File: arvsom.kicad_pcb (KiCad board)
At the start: 12 copper layers, 55 x 40 mm, 414 parts, among them J3 DF40C-100DP-0.4V(51), J4 DF40C-100DP-0.4V(51), Q5 BSS138AKA, U1 MT53D1024M32D4DT-053, U10 TDA19988BHN_C1,557, U11 KSZ9031RNXCA, U13 VIC7100, U2 GD25LQ256DWIGR, U3 MT53D1024M32D4DT-053, U4 CSD86330Q3D, U5 LMR62014XMF_NOPB, U6 CSD86330Q3D, U8 TPS65086100, Y1 ABM8G-25.000MHZ-18-D2Y-T

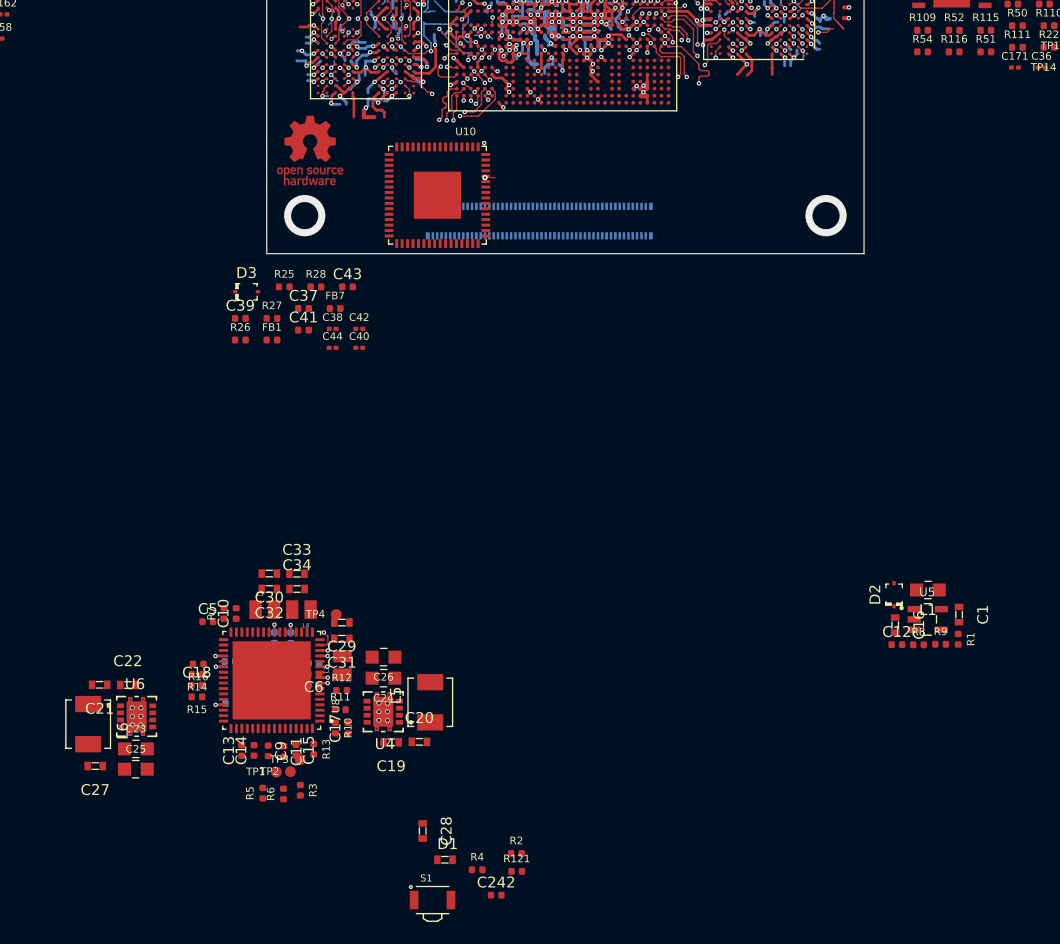
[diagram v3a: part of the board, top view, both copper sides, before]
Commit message: PMIC initial placement
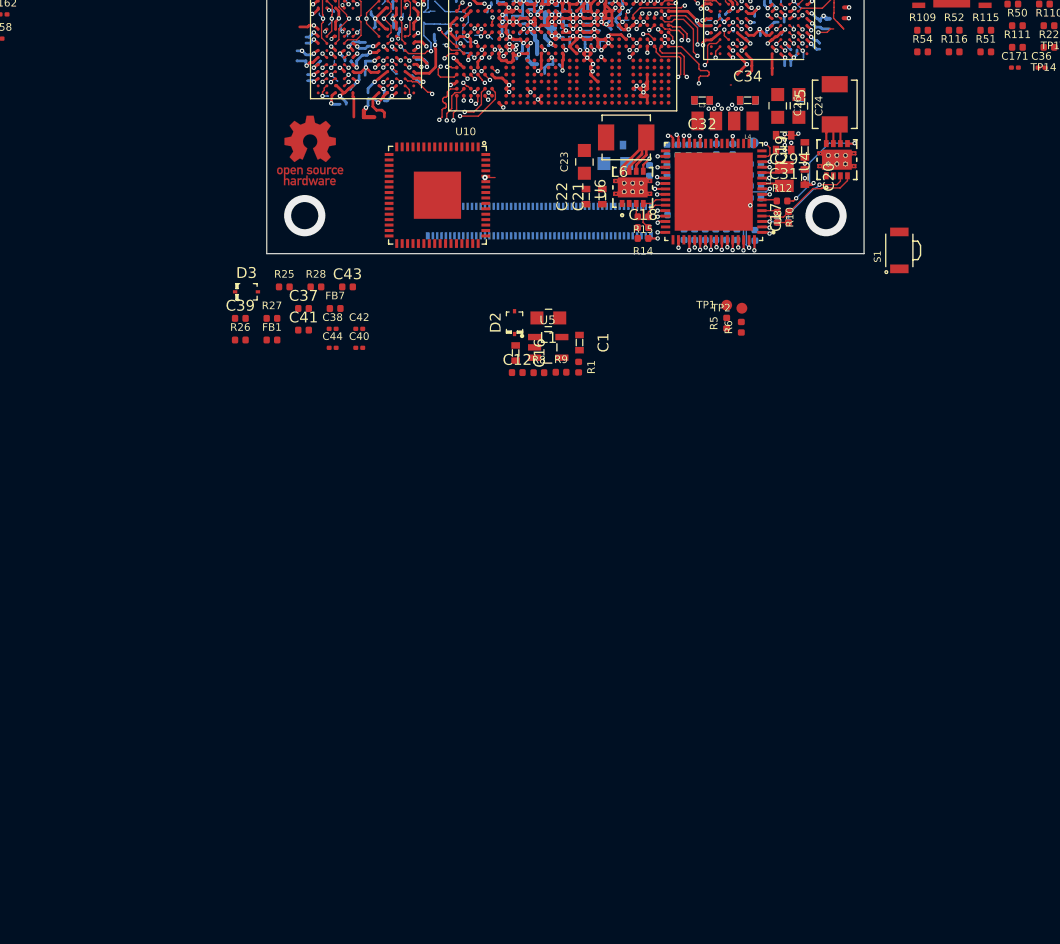
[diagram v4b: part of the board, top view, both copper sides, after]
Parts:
- C10, C11, C13, C14, C15, C242, C25, C27, C28, C30, C33, C5, C6, C9, D1, R11, R121, R13, R16, R2, R3, R4, R7, TP3, TP4: moved to B.Cu
- moved C28 75.2 mm to (179.2, 81.4)
- moved C27 74.6 mm to (162.1, 85.0), turned to 0 degrees
- moved S1 73.7 mm to (188.3, 94.7), turned to 90 degrees
- moved L6 73.3 mm to (163.1, 84.3), turned to 180 degrees
- moved C242 71.4 mm to (175.0, 86.7), turned to 180 degrees
- moved C25 71.1 mm to (162.1, 86.7)
- moved C23 68.0 mm to (159.3, 86.5), turned to 90 degrees
- moved R2 66.9 mm to (169.9, 85.4), turned to 90 degrees
- moved R121 66.8 mm to (173.0, 88.1), turned to 90 degrees
- moved U6 66.8 mm to (163.7, 88.9), turned to 90 degrees
- moved C19 66.5 mm to (179.6, 85.4), turned to 90 degrees
- moved L5 66.5 mm to (182.3, 81.2)
- moved D1 65.8 mm to (171.7, 90.0), turned to 270 degrees
- moved U4 65.8 mm to (182.5, 86.3), turned to 90 degrees
- moved R4 65.8 mm to (173.0, 90.3), turned to 270 degrees
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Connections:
- C12 pad 1: VCC_5V8 -> VSYS_5V8
- C16 pad 1: VCC_5V8 -> VSYS_5V8
- C45 pad 1: VCC1V2 -> VCC_1V2
- C46 pad 1: VCC1V2 -> VCC_1V2
- C48 pad 1: VCC1V2 -> VCC_1V2
- C49 pad 1: VCC3V3 -> VCC_3V3
- C52 pad 1: VCC1V2 -> VCC_1V2
- C53 pad 1: VCC3V3 -> VCC_3V3
- C56 pad 1: VCC1V2 -> VCC_1V2
- C57 pad 1: VCC3V3 -> VCC_3V3
- C61 pad 1: VCC1V2 -> VCC_1V2
- C62 pad 1: VCC3V3 -> VCC_3V3
- C64 pad 1: VCC1V2 -> VCC_1V2
- C65 pad 1: VCC3V3 -> VCC_3V3
- C67 pad 1: VCC1V2 -> VCC_1V2
- C68 pad 1: VCC1V2 -> VCC_1V2
- D2 pad K: VCC_5V8 -> VSYS_5V8
- FB2 pad 1: VCC3V3 -> VCC_3V3
- FB3 pad 1: VCC1V2 -> VCC_1V2
- FB4 pad 1: VCC1V2 -> VCC_1V2
- R31 pad 2: VCC3V3 -> VCC_3V3
- R32 pad 2: VCC3V3 -> VCC_3V3
- R33 pad 2: VCC3V3 -> VCC_3V3
- R34 pad 2: VCC3V3 -> VCC_3V3
- R35 pad 2: VCC3V3 -> VCC_3V3
- R36 pad 2: VCC3V3 -> VCC_3V3
- R37 pad 2: VCC3V3 -> VCC_3V3
- R38 pad 2: VCC3V3 -> VCC_3V3
- R39 pad 2: VCC3V3 -> VCC_3V3
- R40 pad 2: VCC3V3 -> VCC_3V3
- R8 pad 1: VCC_5V8 -> VSYS_5V8
- U11 pad 14: VCC1V2 -> VCC_1V2
- U11 pad 16: VCC3V3 -> VCC_3V3
- U11 pad 18: VCC1V2 -> VCC_1V2
- U11 pad 23: VCC1V2 -> VCC_1V2
- U11 pad 26: VCC1V2 -> VCC_1V2
- U11 pad 30: VCC1V2 -> VCC_1V2
- U11 pad 34: VCC3V3 -> VCC_3V3
- U11 pad 39: VCC1V2 -> VCC_1V2
- U11 pad 40: VCC3V3 -> VCC_3V3
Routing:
- net Net-(C18-Pad2): track 0.00 -> 15.9 mm
- net Net-(C17-Pad2): track 0.00 -> 15.6 mm
- net Net-(R12-Pad2): track 0.00 -> 10.3 mm, vias 0 -> 2
- net GND: track 410.0 -> 417.9 mm, vias 229 -> 241
- net Net-(R11-Pad2): track 0.00 -> 7.28 mm, vias 0 -> 1
- net VCC_3V3: track 28.8 -> 34.6 mm, vias 7 -> 13
- net Net-(TP3-Pad1): track 0.00 -> 4.16 mm, vias 0 -> 1
- net CTL5: track 0.00 -> 3.89 mm, vias 0 -> 1
- net LDO_3V3: track 0.70 -> 3.50 mm
- net Net-(R15-Pad1): track 0.00 -> 2.36 mm
- net Net-(L2-Pad1): track 0.00 -> 2.15 mm
- net VCC_5V0: track 3.48 -> 5.27 mm, vias 5 -> 7
- net Net-(R14-Pad1): track 0.00 -> 1.64 mm, vias 0 -> 2
- net Net-(R11-Pad1): track 0.00 -> 1.49 mm, vias 0 -> 1
- net VCC_1V1: track 71.9 -> 73.3 mm, vias 32 -> 34
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
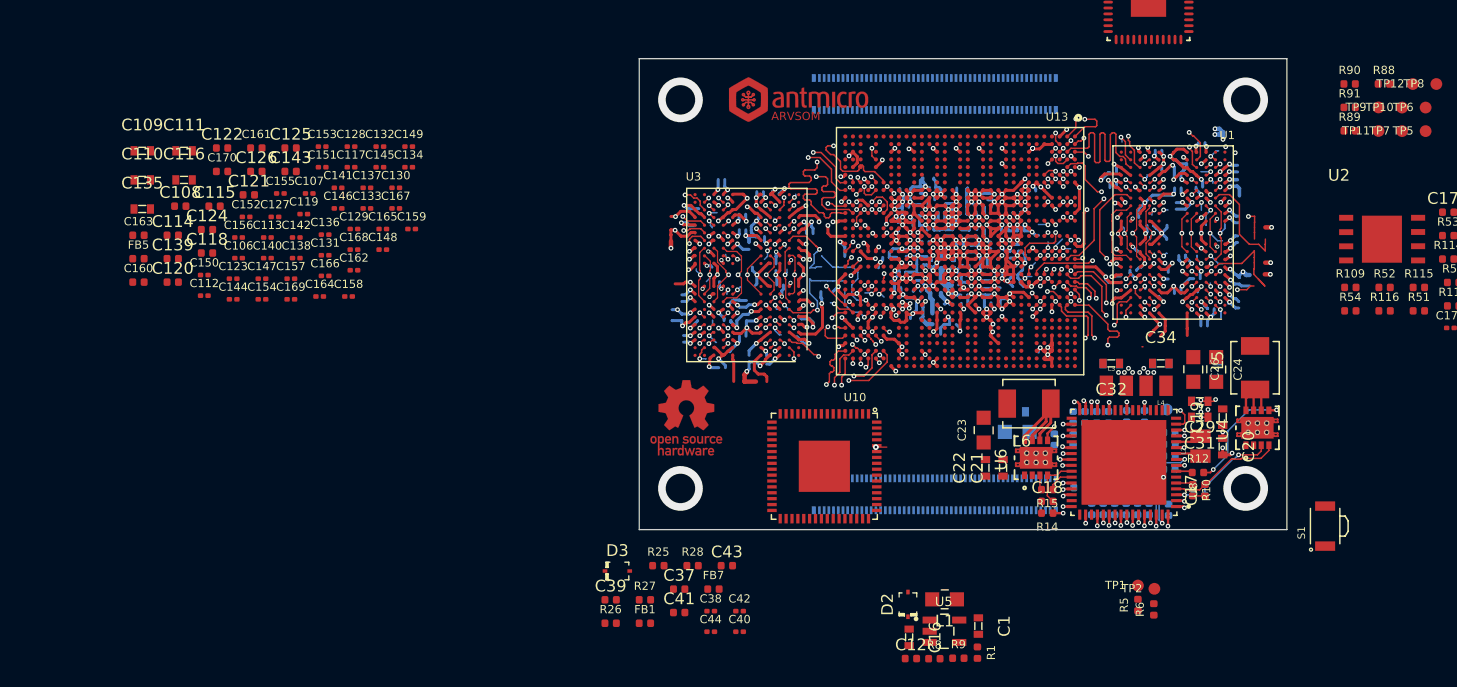
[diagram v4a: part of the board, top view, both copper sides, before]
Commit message: Updated VIC config, added reset and crystals
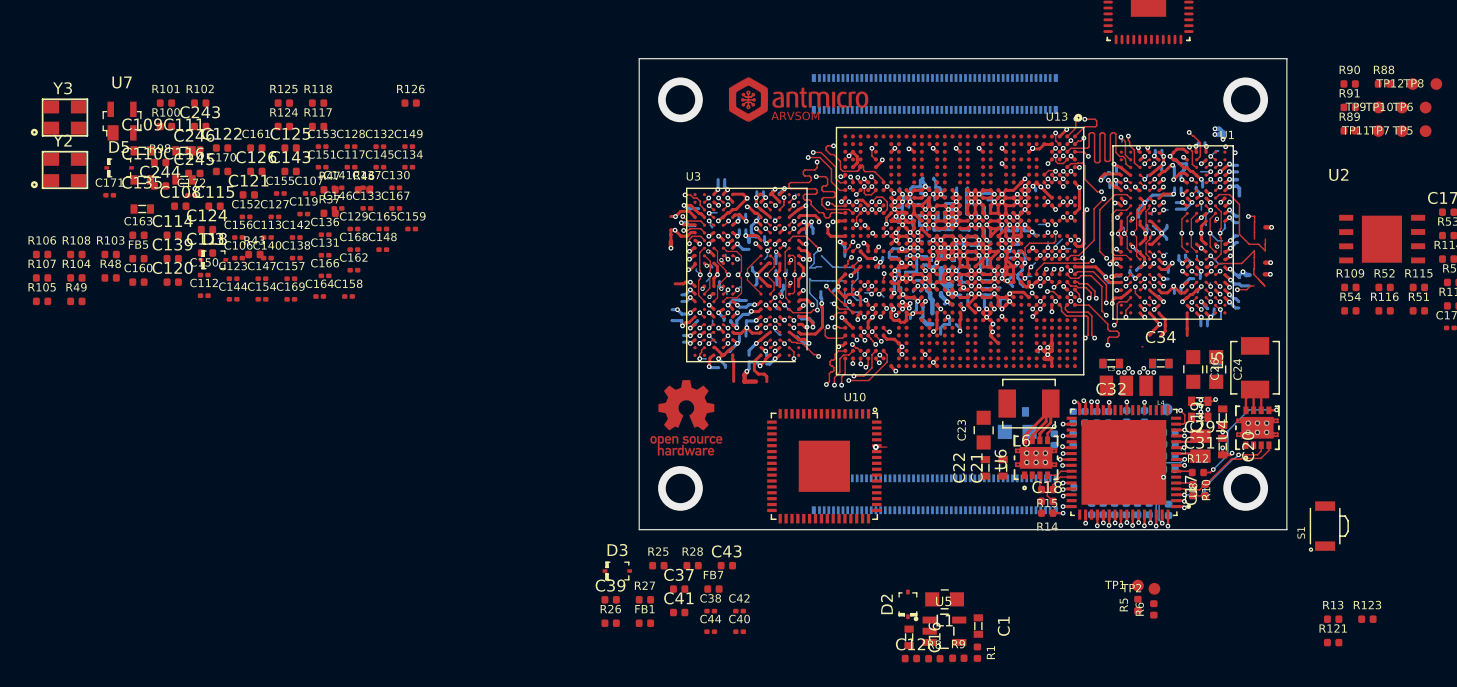
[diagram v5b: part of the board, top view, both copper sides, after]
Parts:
- added C171: C_100n_0201, arvsom-footprints:0201-res, F.Cu at (85.0, 66.6)
- added C172: C_100n_0201, arvsom-footprints:0201-res, F.Cu at (92.0, 66.6)
- added C243: C_10p_0402, arvsom-footprints:0402-cap, F.Cu at (92.7, 60.7)
- added C244: C_10p_0402, arvsom-footprints:0402-cap, F.Cu at (89.3, 65.8)
- added C245: C_10p_0402, arvsom-footprints:0402-cap, F.Cu at (92.2, 64.7)
- added C246: C_10p_0402, arvsom-footprints:0402-cap, F.Cu at (92.2, 62.7)
- added D3: PMEG3010CEJ, arvsom-footprints:SOD-323F, F.Cu at (93.9, 72.1)
- added D5: PMEG3010CEJ, arvsom-footprints:SOD-323F, F.Cu at (85.8, 64.3)
- added R100: R_1M0_0402, arvsom-footprints:0402-res, F.Cu at (89.8, 60.7)
- added R101: R_0R_0402, arvsom-footprints:0402-res, F.Cu at (89.8, 58.7)
- added R102: R_0R_0402, arvsom-footprints:0402-res, F.Cu at (92.7, 58.7)
- added R103: R_10k_0402, arvsom-footprints:0402-res, F.Cu at (85.1, 71.6)
- added R104: R_10k_0402, arvsom-footprints:0402-res, F.Cu at (82.2, 73.6)
- added R105: R_10k_0402, arvsom-footprints:0402-res, F.Cu at (79.3, 75.6)
- added R106: R_10k_0402, arvsom-footprints:0402-res, F.Cu at (79.3, 71.6)
- added R107: R_10k_0402, arvsom-footprints:0402-res, F.Cu at (79.3, 73.6)
- added R108: R_10k_0402, arvsom-footprints:0402-res, F.Cu at (82.2, 71.6)
- added R117: R_4k7_0402, arvsom-footprints:0402-res, F.Cu at (102.7, 60.7)
- added R118: R_4k7_0402, arvsom-footprints:0402-res, F.Cu at (102.7, 58.7)
- added R121: R_1k_0402, arvsom-footprints:0402-res, F.Cu at (188.9, 104.6)
- added R123: R_0R_0402, arvsom-footprints:0402-res, F.Cu at (191.9, 102.6)
- added R124: R_4k7_0402, arvsom-footprints:0402-res, F.Cu at (99.8, 60.7)
- added R125: R_4k7_0402, arvsom-footprints:0402-res, F.Cu at (99.8, 58.7)
- added R126: R_100k_0402, arvsom-footprints:0402-res, F.Cu at (110.6, 58.7)
- added R13: R_12k1_0402, arvsom-footprints:0402-res, F.Cu at (188.9, 102.6)
- added R37: R_1k_0402, arvsom-footprints:0402-res, F.Cu at (103.7, 68.1)
- added R43: R_10k_0402, arvsom-footprints:0402-res, F.Cu at (97.3, 71.6)
- added R46: R_0R_0402, arvsom-footprints:0402-res, F.Cu at (106.6, 66.1)
- added R47: R_0R_0402, arvsom-footprints:0402-res, F.Cu at (103.7, 66.1)
- added R48: R_0R_0402, arvsom-footprints:0402-res, F.Cu at (85.1, 73.6)
- added R49: R_10k_0402, arvsom-footprints:0402-res, F.Cu at (82.2, 75.6)
- added R98: R_1M0_0402, arvsom-footprints:0402-res, F.Cu at (89.3, 63.8)
- added U7: STM811RW16F, arvsom-footprints:SOT-143-4, F.Cu at (86.1, 60.3)
- added Y2: ABM8G-25.000MHZ-18-D2Y-T, arvsom-footprints:KX-7, F.Cu at (81.2, 64.4)
- added Y3: ABM8G-27.000MHZ-18-D2Y-T, arvsom-footprints:KX-7, F.Cu at (81.2, 59.9)
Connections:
- net Net-(U13-PadA25) renamed JTAG_TDO
- net Net-(U13-PadA26) renamed JTAG_TMS
- net Net-(U13-PadC25) renamed JTAG_TDI
- net Net-(U13-PadE26) renamed UART3_TXD_1V8
- net Net-(U13-PadG23) renamed JTAG_TRSTN
- net Net-(U13-PadH22) renamed JTAG_TCK
- net Net-(U13-PadH24) renamed UART3_RXD_1V8
- net PWR_OFF renamed Net-(U13-PadN5)
- net RPI_GPIO14 renamed GPIO14
- net RPI_GPIO15 renamed GPIO13
- net RPI_GPIO8 renamed GPIO15
- C100 pad 1: VDD2 -> VCC_1V1
- C101 pad 1: VDD1 -> VCC_1V8
- C102 pad 1: VDD2 -> VCC_1V1
- C103 pad 1: VDD2 -> VCC_1V1
- C104 pad 1: VDD2 -> VCC_1V1
- C105 pad 1: VDD2 -> VCC_1V1
- C207 pad 1: VDD2 -> VCC_1V1
- C208 pad 1: VDDQ -> VCC_1V1
- C209 pad 1: VDD2 -> VCC_1V1
- C210 pad 1: VDD2 -> VCC_1V1
- C211 pad 1: VDDQ -> VCC_1V1
- C212 pad 1: VDD2 -> VCC_1V1
- C213 pad 1: VDDQ -> VCC_1V1
- C214 pad 1: VDDQ -> VCC_1V1
- C215 pad 1: VDD2 -> VCC_1V1
- C216 pad 1: VDD2 -> VCC_1V1
- C217 pad 1: VDDQ -> VCC_1V1
- C218 pad 1: VDD1 -> VCC_1V8
- C219 pad 1: VDDQ -> VCC_1V1
- C220 pad 1: VDD2 -> VCC_1V1
- C221 pad 1: VDD2 -> VCC_1V1
- C222 pad 1: VDDQ -> VCC_1V1
- C223 pad 1: VDD1 -> VCC_1V8
- C224 pad 1: VDDQ -> VCC_1V1
- C225 pad 1: VDD2 -> Net-(C225-Pad1)
- C226 pad 1: VDD2 -> VCC_1V1
- C227 pad 1: VDDQ -> VCC_1V1
- C228 pad 1: VDD1 -> VCC_1V8
- C229 pad 1: VDDQ -> VCC_1V1
- C23 pad 1: VCC_1V1 -> VCC_0V9
- C230 pad 1: VDD2 -> Net-(C230-Pad1)
- C231 pad 1: VDD2 -> VCC_1V1
- C232 pad 1: VDDQ -> VCC_1V1
- C233 pad 1: VDD1 -> VCC_1V8
- C234 pad 1: VDDQ -> VCC_1V1
- C235 pad 1: VDD2 -> VCC_1V1
- C236 pad 1: VDD2 -> VCC_1V1
- C237 pad 1: VDDQ -> VCC_1V1
- C238 pad 1: VDD1 -> VCC_1V8
- C239 pad 1: VDDQ -> VCC_1V1
- C24 pad 1: VCC_0V9 -> VCC_1V1
- C240 pad 1: VDD2 -> VCC_1V1
- C241 pad 1: VDD2 -> VCC_1V1
- C242 pad 1: PWR_EN -> SYS_RSTN
- C25 pad 1: VCC_1V1 -> VCC_0V9
- C26 pad 1: VCC_0V9 -> VCC_1V1
- C27 pad 1: VCC_1V1 -> VCC_0V9
- C28 pad 1: VCC_0V9 -> VCC_1V1
- C71 pad 1: VDDQ -> VCC_1V1
- C72 pad 1: VDDQ -> VCC_1V1
- C73 pad 1: VDD2 -> VCC_1V1
- C74 pad 1: VDDQ -> VCC_1V1
- C75 pad 1: VDDQ -> VCC_1V1
- C76 pad 1: VDD2 -> VCC_1V1
- C77 pad 1: VDDQ -> VCC_1V1
- C78 pad 1: VDDQ -> VCC_1V1
- C79 pad 1: VDD2 -> VCC_1V1
- C80 pad 1: VDDQ -> VCC_1V1
- C81 pad 1: VDDQ -> VCC_1V1
- C82 pad 1: VDD2 -> VCC_1V1
- C83 pad 1: VDDQ -> VCC_1V1
- C84 pad 1: VDDQ -> VCC_1V1
- C85 pad 1: VDD2 -> VCC_1V1
- C86 pad 1: VDDQ -> VCC_1V1
- C87 pad 1: VDDQ -> VCC_1V1
- C88 pad 1: VDD2 -> VCC_1V1
- C89 pad 1: VDDQ -> VCC_1V1
- C90 pad 1: VDD2 -> VCC_1V1
- C91 pad 1: VDDQ -> VCC_1V1
- C92 pad 1: VDD2 -> VCC_1V1
- C93 pad 1: VDD2 -> VCC_1V1
- C94 pad 1: VDD1 -> VCC_1V8
- C95 pad 1: VDD1 -> VCC_1V8
- C96 pad 1: VDD2 -> VCC_1V1
- C97 pad 1: VDD1 -> VCC_1V8
- C98 pad 1: VDD2 -> VCC_1V1
- C99 pad 1: VDD1 -> VCC_1V8
- J3 pad 21: LED -> GP43_LED
- J3 pad 24: RPI_GPIO26 -> GPIO1
- J3 pad 25: RPI_GPIO21 -> GPIO0
- J3 pad 26: RPI_GPIO19 -> GPIO3
- J3 pad 27: RPI_GPIO20 -> GPIO2
- J3 pad 28: RPI_GPIO13 -> GPIO5
- J3 pad 29: RPI_GPIO16 -> GPIO4
- J3 pad 30: RPI_GPIO6 -> GPIO6
- J3 pad 31: RPI_GPIO12 -> GPIO7
- J3 pad 34: RPI_GPIO5 -> GPIO8
- J3 pad 35: RPI_ID_SC -> GPIO10
- J3 pad 36: RPI_ID_SD -> GPIO9
- J3 pad 37: RPI_GPIO7 -> GPIO11
- J3 pad 38: RPI_GPIO11 -> GPIO12
- J3 pad 40: RPI_GPIO9 -> GPIO16
- J3 pad 41: RPI_GPIO25 -> GPIO17
- J3 pad 44: RPI_GPIO10 -> GPIO18
- J3 pad 45: RPI_GPIO24 -> GPIO19
- J3 pad 46: RPI_GPIO22 -> GPIO20
- J3 pad 47: RPI_GPIO23 -> GPIO21
- J3 pad 48: RPI_GPIO27 -> GPIO22
- J3 pad 49: RPI_GPIO18 -> GPIO45
- J3 pad 50: RPI_GPIO17 -> GPIO44
- J3 pad 54: RPI_GPIO4 -> GPIO46
- J3 pad 56: RPI_GPIO3 -> GPIO47
- J3 pad 58: RPI_GPIO2 -> GPIO48
- J4 pad 10: PCIE_CLK_P -> RES_SSTX2_P
- J4 pad 12: PCIE_CLK_N -> RES_SSTX2_N
- J4 pad 16: PCIE_RX_P -> USB_SSRX1_P
- J4 pad 18: PCIE_RX_N -> USB_SSRX1_N
- J4 pad 22: PCIE_TX_P -> USB_SSTX1P
- J4 pad 24: PCIE_TX_N -> USB_SSTX1N
- J4 pad 4: RESERVED -> RES_SSRX2_P
- J4 pad 57: DSI1_D0_N -> CDTX_DSI_D0_N
- J4 pad 59: DSI1_D0_P -> CDTX_DSI_D0_P
- J4 pad 6: RESERVED -> RES_SSRX2_N
- J4 pad 63: DSI1_D1_N -> CDTX_DSI_D1_N
- J4 pad 65: DSI1_D1_P -> CDTX_DSI_D1_P
- J4 pad 69: DSI0_C_N -> CDTX_DSI_CK_N
- J4 pad 71: DSI0_C_P -> CDTX_DSI_CK_P
- J4 pad 75: CDTX_DSI_D0_N -> DSI1_D0_N
- J4 pad 77: CDTX_DSI_D0_P -> DSI1_D0_P
- J4 pad 81: CDTX_DSI_D1_N -> DSI1_D1_N
- J4 pad 83: CDTX_DSI_D1_P -> DSI1_D1_P
- J4 pad 87: CDTX_DSI_D2_N -> DSI1_C_N
- J4 pad 89: CDTX_DSI_D2_P -> DSI1_C_P
- J4 pad 93: CDTX_DSI_D3_N -> DSI1_D2_N
- J4 pad 94: CDTX_DSI_D4_N -> DSI1_D3_N
- J4 pad 95: CDTX_DSI_D3_P -> DSI1_D2_P
- J4 pad 96: CDTX_DSI_D4_P -> DSI1_D3_P
- L5 pad 2: VCC_0V9 -> VCC_1V1
- L6 pad 2: VCC_1V1 -> VCC_0V9
- R119 pad 1: LED -> GP43_LED
- R122 pad 2: SDIO0_CD -> GPIO55_GMAC_RESETN
- R38 pad 1: ETH_~RESET -> RGMII_MDC
- R42 pad 2: VDDQ -> VCC_1V1
- R44 pad 1: VDDQ -> VCC_1V1
- R44 pad 2: DDR0_ODT_1 -> DDR0_ODT1
- R45 pad 2: VDDQ -> VCC_1V1
- R54 pad 2: SYS_RSTN -> VIC_RSTN
- R93 pad 2: DDR0_ODT_1 -> DDR0_ODT1
- R94 pad 1: VDDQ -> VCC_1V1
- R97 pad 2: VDDQ -> VCC_1V1
- R99 pad 2: VDDQ -> VCC_1V1
- U1 pad A4: VDD2 -> VCC_1V1
- U1 pad A9: VDD2 -> VCC_1V1
- U1 pad AA10: VDDQ -> VCC_1V1
- U1 pad AA3: VDDQ -> VCC_1V1
- U1 pad AA5: VDDQ -> VCC_1V1
- U1 pad AA8: VDDQ -> VCC_1V1
- U1 pad AB4: VDD2 -> VCC_1V1
- U1 pad AB9: VDD2 -> VCC_1V1
- U1 pad B10: VDDQ -> VCC_1V1
- U1 pad B3: VDDQ -> VCC_1V1
- U1 pad B5: VDDQ -> VCC_1V1
- U1 pad B8: VDDQ -> VCC_1V1
- U1 pad D1: VDDQ -> VCC_1V1
- U1 pad D10: DDR0_DQS1N -> DDR0_DQS1P
- U1 pad D12: VDDQ -> VCC_1V1
- U1 pad D3: DDR0_DQS0N -> DDR0_DQS0P
- U1 pad D5: VDDQ -> VCC_1V1
- U1 pad D8: VDDQ -> VCC_1V1
- U1 pad E10: DDR0_DQS1P -> DDR0_DQS1N
- U1 pad E3: DDR0_DQS0P -> DDR0_DQS0N
- U1 pad F1: VDD1 -> VCC_1V8
- U1 pad F10: VDDQ -> VCC_1V1
- U1 pad F12: VDD1 -> VCC_1V8
- U1 pad F3: VDDQ -> VCC_1V1
- U1 pad F5: VDD2 -> VCC_1V1
- U1 pad F8: VDD2 -> VCC_1V1
- U1 pad G2: Net-(R43-Pad2) -> DDR0_ODT_0
- U1 pad G4: VDD1 -> VCC_1V8
- U1 pad G9: VDD1 -> VCC_1V8
- U1 pad H1: VDD2 -> VCC_1V1
- U1 pad H12: VDD2 -> VCC_1V1
- U1 pad H5: VDD2 -> VCC_1V1
- U1 pad H8: VDD2 -> VCC_1V1
- U1 pad J8: DDR0_CK0_N -> DDR0_CK0_P
- U1 pad J9: DDR0_CK0_P -> DDR0_CK0_N
- U1 pad K1: VDD2 -> VCC_1V1
- U1 pad K10: VDD2 -> VCC_1V1
- U1 pad K12: VDD2 -> VCC_1V1
- U1 pad K3: VDD2 -> VCC_1V1
- U1 pad N1: VDD2 -> VCC_1V1
- U1 pad N10: VDD2 -> VCC_1V1
- U1 pad N12: VDD2 -> VCC_1V1
- U1 pad N3: VDD2 -> VCC_1V1
- U1 pad P8: DDR0_CK1_N -> DDR0_CK1_P
- U1 pad P9: DDR0_CK1_P -> DDR0_CK1_N
- U1 pad R1: VDD2 -> VCC_1V1
- U1 pad R12: VDD2 -> VCC_1V1
- U1 pad R5: VDD2 -> VCC_1V1
- U1 pad R8: VDD2 -> VCC_1V1
- U1 pad T11: Net-(R47-Pad2) -> DDR0_RSTN
- U1 pad T4: VDD1 -> VCC_1V8
- U1 pad T9: VDD1 -> VCC_1V8
- U1 pad U1: VDD1 -> VCC_1V8
- U1 pad U10: VDDQ -> VCC_1V1
- U1 pad U12: VDD1 -> VCC_1V8
- U1 pad U3: VDDQ -> VCC_1V1
- U1 pad U5: VDD2 -> VCC_1V1
- U1 pad U8: VDD2 -> VCC_1V1
- U1 pad V10: DDR0_DQS3P -> DDR0_DQS3N
- U1 pad V3: DDR0_DQS2P -> DDR0_DQS2N
- U1 pad W1: VDDQ -> VCC_1V1
- U1 pad W10: DDR0_DQS3N -> DDR0_DQS3P
- U1 pad W12: VDDQ -> VCC_1V1
- U1 pad W3: DDR0_DQS2N -> DDR0_DQS2P
- U1 pad W5: VDDQ -> VCC_1V1
- U1 pad W8: VDDQ -> VCC_1V1
- U11 pad 42: ETH_~RESET -> /Ethernet/ETH_RESETn
- U13 pad AC26: Net-(U13-PadAC26) -> USB_SSTX1N
- U13 pad AC27: Net-(U13-PadAC27) -> USB_SSTX1P
- U13 pad AC30: Net-(U13-PadAC30) -> RES_SSRX2_N
- U13 pad AC31: Net-(U13-PadAC31) -> RES_SSRX2_P
- U13 pad AD26: Net-(U13-PadAD26) -> USB_SSRX1_N
- U13 pad AD27: Net-(U13-PadAD27) -> USB_SSRX1_P
- U13 pad AD30: Net-(U13-PadAD30) -> RES_SSTX2_P
- U13 pad AD31: Net-(U13-PadAD31) -> RES_SSTX2_N
- U13 pad D1: RPI_GPIO3 -> GPIO1
- U13 pad E1: RPI_GPIO2 -> GPIO0
- U13 pad F1: RPI_GPIO11 -> GPIO6
- U13 pad F2: RPI_GPIO4 -> GPIO2
- U13 pad F4: RPI_ID_SC -> GPIO17
- U13 pad F5: RPI_GPIO9 -> GPIO12
- U13 pad F6: RPI_GPIO22 -> GPIO5
- U13 pad G1: RPI_GPIO25 -> GPIO7
- U13 pad G2: RPI_GPIO17 -> GPIO3
- U13 pad G4: RPI_GPIO6 -> GPIO20
- U13 pad G5: RPI_GPIO23 -> GPIO9
- U13 pad G6: RPI_GPIO27 -> GPIO4
- U13 pad H1: RPI_GPIO10 -> GPIO11
- U13 pad H2: RPI_GPIO24 -> GPIO10
- U13 pad H4: RPI_GPIO16 -> Net-(R57-Pad2)
- U13 pad J1: RPI_GPIO19 -> GPIO22
- U13 pad J2: RPI_ID_SD -> GPIO18
- U13 pad J30: CDTX_DSI_D2_N -> CDTX_DSI_CK_N
- U13 pad J31: CDTX_DSI_D2_P -> CDTX_DSI_CK_P
- U13 pad J5: RPI_GPIO12 -> GPIO24
- U13 pad J6: RPI_GPIO7 -> GPIO16
- U13 pad J7: RPI_GPIO18 -> GPIO8
- U13 pad K1: RPI_GPIO21 -> Net-(R56-Pad2)
- U13 pad K2: RPI_GPIO26 -> GPIO23
- U13 pad K30: CDTX_DSI_D3_N -> Net-(U13-PadK30)
- U13 pad K31: CDTX_DSI_D3_P -> Net-(U13-PadK31)
- U13 pad K4: RPI_GPIO5 -> GPIO19
- U13 pad K6: RPI_GPIO13 -> GPIO21
- U13 pad L1: RPI_GPIO20 -> Net-(R59-Pad2)
- U13 pad L29: SYS_RSTN -> VIC_RSTN
- U13 pad L30: CDTX_DSI_D4_N -> Net-(U13-PadL30)
- U13 pad L31: CDTX_DSI_D4_P -> Net-(U13-PadL31)
- U13 pad M1: LED -> Net-(U13-PadM1)
- U13 pad M5: Net-(U13-PadM5) -> Net-(R58-Pad2)
- U13 pad M6: VDD2PEN -> Net-(R55-Pad2)
- U13 pad N1: Net-(U13-PadN1) -> GP43_LED
- U13 pad R1: SDIO0_CD -> SDIO0_D1
- U13 pad R2: SDIO0_D3 -> GPIO47
- U13 pad R3: SDIO0_D2 -> GPIO46
- U13 pad R30: CSI2RX_CLK_N -> CSI2RX_D1_N
- U13 pad R31: CSI2RX_CLK_P -> CSI2RX_D1_P
- U13 pad R4: SDIO0_D1 -> GPIO45
- U13 pad R5: SDIO0_D0 -> GPIO44
- U13 pad T1: CSI1_PWDN -> SDIO0_D2
- U13 pad T2: CSI0_PWDN -> SDIO0_D3
- U13 pad T30: CSI2RX_D1_N -> CSI2RX_D0_N
- U13 pad T31: CSI2RX_D1_P -> CSI2RX_D0_P
- U13 pad T4: I2C0_SDA -> GPIO55_GMAC_RESETN
- U13 pad T5: I2C2_SDA -> SDIO0_CMD
- U13 pad T6: SDIO0_CLK -> SDIO0_D0
- U13 pad T7: SDIO0_CMD -> GPIO48
- U13 pad U1: I2C2_SCL -> SDIO0_CLK
- U13 pad U30: CSI2RX_D0_N -> CSI2RX_CLK_N
- U13 pad U31: CSI2RX_D0_P -> CSI2RX_CLK_P
- U13 pad V1: I2C0_SCL -> VDD2PEN
- U13 pad V2: Net-(U13-PadV2) -> CSI1_PWDN
- U13 pad V3: Net-(R56-Pad2) -> I2C2_SCL
- U13 pad V4: Net-(R57-Pad2) -> I2C0_SDA
- U13 pad V5: Net-(R55-Pad2) -> I2C2_SDA
- U13 pad V6: Net-(U13-PadV6) -> CSI0_PWDN
- U13 pad V7: Net-(R59-Pad2) -> GPIO63_GMAC_RESETN
- U13 pad W5: Net-(R58-Pad2) -> I2C0_SCL
- U3 pad A4: VDD2 -> VCC_1V1
- U3 pad A9: VDD2 -> VCC_1V1
- U3 pad AA10: VDDQ -> VCC_1V1
- U3 pad AA3: VDDQ -> VCC_1V1
- U3 pad AA5: VDDQ -> VCC_1V1
- U3 pad AA8: VDDQ -> VCC_1V1
- U3 pad AB4: VDD2 -> VCC_1V1
- U3 pad AB9: VDD2 -> VCC_1V1
- U3 pad B10: VDDQ -> VCC_1V1
- U3 pad B3: VDDQ -> VCC_1V1
- U3 pad B5: VDDQ -> VCC_1V1
- U3 pad B8: VDDQ -> VCC_1V1
- U3 pad D1: VDDQ -> VCC_1V1
- U3 pad D10: DDR1_DQS1N -> DDR1_DQS1P
- U3 pad D12: VDDQ -> VCC_1V1
- U3 pad D3: DDR1_DQS0N -> DDR1_DQS0P
- U3 pad D5: VDDQ -> VCC_1V1
- U3 pad D8: VDDQ -> VCC_1V1
- U3 pad E10: DDR1_DQS1P -> DDR1_DQS1N
- U3 pad E3: DDR1_DQS0P -> DDR1_DQS0N
- U3 pad F1: VDD1 -> VCC_1V8
- U3 pad F10: VDDQ -> VCC_1V1
- U3 pad F12: VDD1 -> VCC_1V8
- U3 pad F3: VDDQ -> VCC_1V1
- U3 pad F5: VDD2 -> VCC_1V1
- U3 pad F8: VDD2 -> VCC_1V1
- U3 pad G2: Net-(R100-Pad1) -> DDR1_ODT_0
- U3 pad G4: VDD1 -> VCC_1V8
- U3 pad G9: VDD1 -> VCC_1V8
- U3 pad H1: VDD2 -> VCC_1V1
- U3 pad H12: VDD2 -> VCC_1V1
- U3 pad H5: VDD2 -> VCC_1V1
- U3 pad H8: VDD2 -> VCC_1V1
- U3 pad J8: DDR1_CK0_N -> DDR1_CK0_P
- U3 pad J9: DDR1_CK0_P -> DDR1_CK0_N
- U3 pad K1: VDD2 -> VCC_1V1
- U3 pad K10: VDD2 -> VCC_1V1
- U3 pad K12: VDD2 -> VCC_1V1
- U3 pad K3: VDD2 -> VCC_1V1
- U3 pad N1: VDD2 -> VCC_1V1
- U3 pad N10: VDD2 -> VCC_1V1
- U3 pad N12: VDD2 -> VCC_1V1
- U3 pad N3: VDD2 -> VCC_1V1
- U3 pad P8: DDR1_CK1_N -> DDR1_CK1_P
- U3 pad P9: DDR1_CK1_P -> DDR1_CK1_N
- U3 pad R1: VDD2 -> VCC_1V1
- U3 pad R12: VDD2 -> VCC_1V1
- U3 pad R5: VDD2 -> VCC_1V1
- U3 pad R8: VDD2 -> VCC_1V1
- U3 pad T11: Net-(R101-Pad2) -> DDR1_RSTN
- U3 pad T4: VDD1 -> VCC_1V8
- U3 pad T9: VDD1 -> VCC_1V8
- U3 pad U1: VDD1 -> VCC_1V8
- U3 pad U10: VDDQ -> VCC_1V1
- U3 pad U12: VDD1 -> VCC_1V8
- U3 pad U3: VDDQ -> VCC_1V1
- U3 pad U5: VDD2 -> VCC_1V1
- U3 pad U8: VDD2 -> VCC_1V1
- U3 pad V10: DDR1_DQS3P -> DDR1_DQS3N
- U3 pad V3: DDR1_DQS2P -> DDR1_DQS2N
- U3 pad W1: VDDQ -> VCC_1V1
- U3 pad W10: DDR1_DQS3N -> DDR1_DQS3P
- U3 pad W12: VDDQ -> VCC_1V1
- U3 pad W3: DDR1_DQS2N -> DDR1_DQS2P
- U3 pad W5: VDDQ -> VCC_1V1
- U3 pad W8: VDDQ -> VCC_1V1
- U8 pad 2: VCC_0V9 -> VCC_1V1
- U8 pad 27: SYS_RSTN -> Net-(R123-Pad2)
- U8 pad 44: VCC_1V1 -> VCC_0V9
- U8 pad 46: VCC_1V1 -> VCC_0V9
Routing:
- net VCC_1V1: track 73.3 -> 182.5 mm, vias 34 -> 111
- net VDD2: track 58.6 -> 0.00 mm, vias 41 -> 0
- net VDDQ: track 53.4 -> 2.15 mm, vias 40 -> 3
- net VCC_1V8: track 25.9 -> 63.0 mm, vias 17 -> 34
- net VDD1: track 37.1 -> 0.00 mm, vias 17 -> 0
- net Net-(R100-Pad1): track 8.61 -> 0.00 mm, vias 1 -> 0
- net DDR1_ODT_0: track 0.00 -> 8.61 mm, vias 0 -> 1
- net Net-(R43-Pad2): track 8.09 -> 0.00 mm
- net DDR0_ODT_0: track 0.00 -> 8.09 mm
- net VCC_0V9: track 61.3 -> 62.0 mm, vias 30 -> 31
- net SYS_RSTN: track 0.69 -> 0.00 mm, vias 1 -> 0
- net Net-(R123-Pad2): track 0.00 -> 0.69 mm, vias 0 -> 1

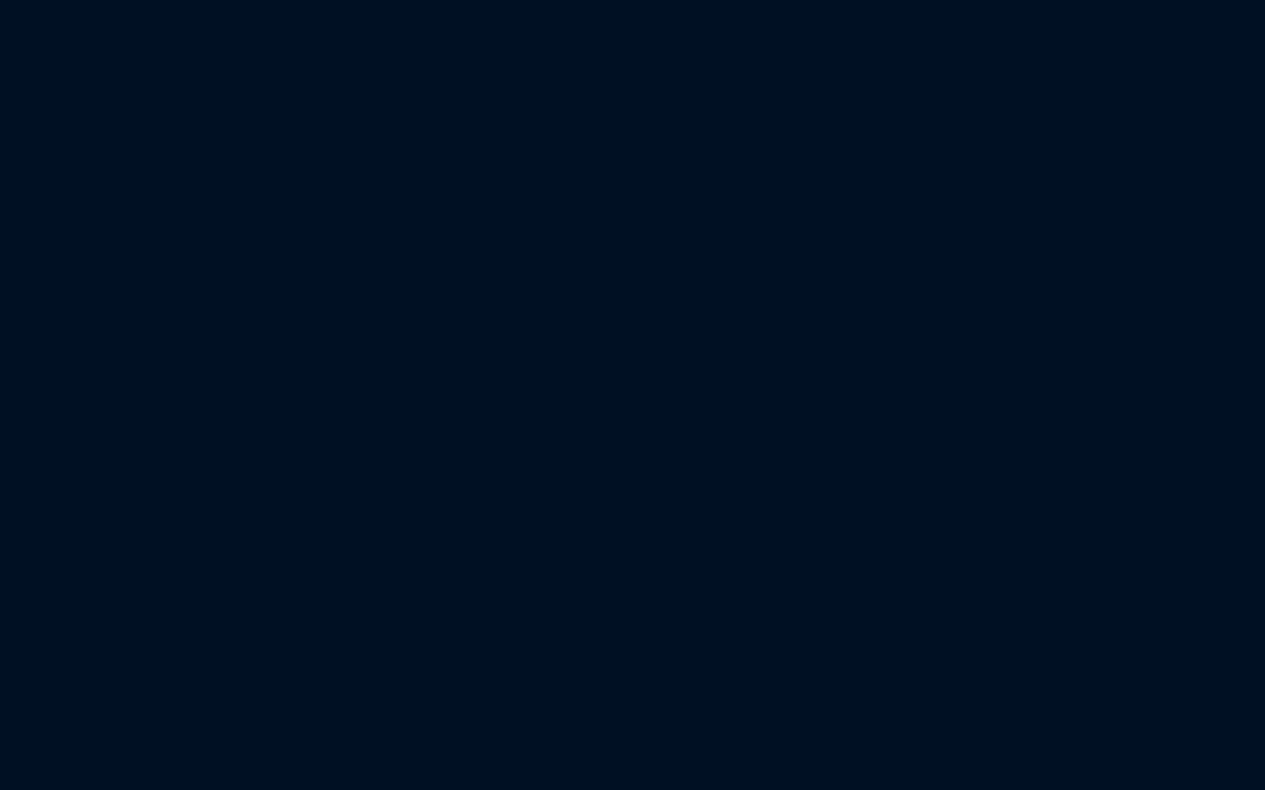
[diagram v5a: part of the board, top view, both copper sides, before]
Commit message: Added JTAG connector
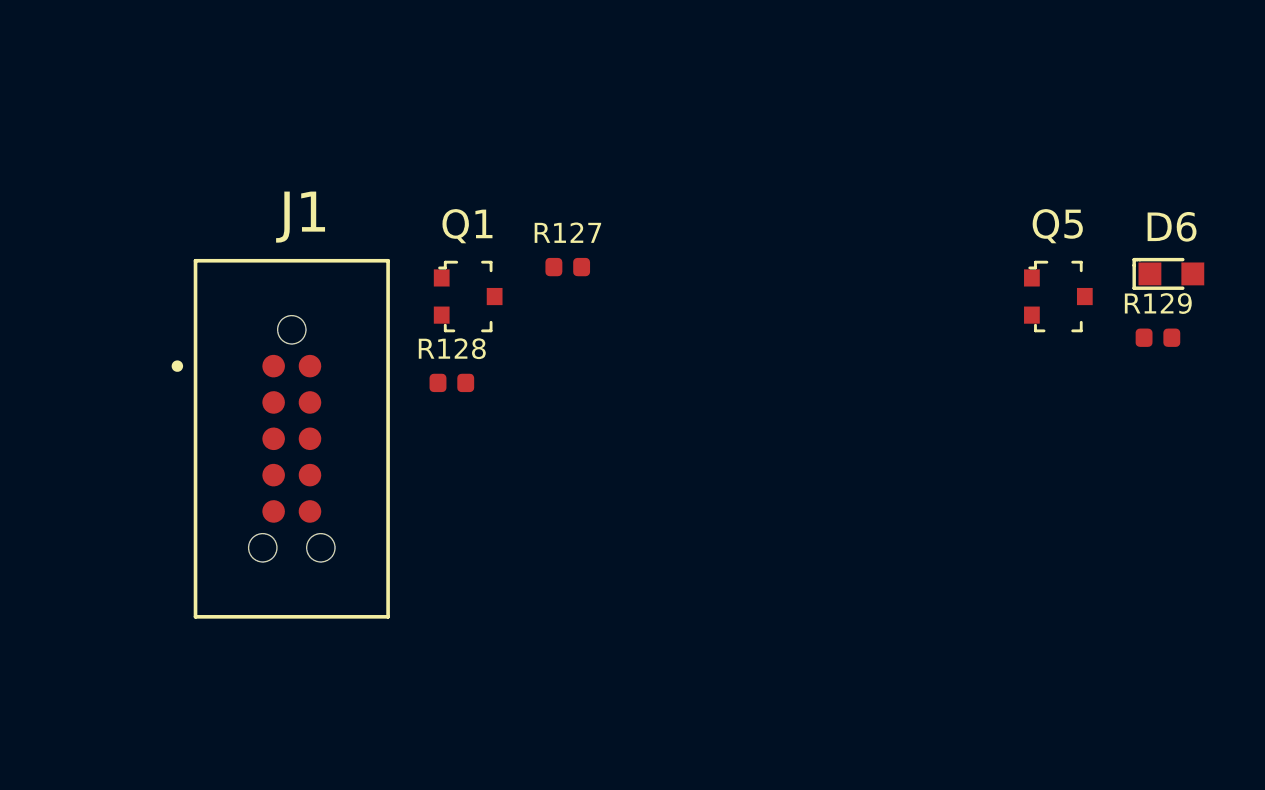
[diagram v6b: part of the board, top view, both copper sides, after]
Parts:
- added D6: KP-1608CGCK, arvsom-footprints:LED_0603, F.Cu at (239.9, 90.2)
- added J1: TAG-10PIN, arvsom-footprints:Tag-Connect_TC2050-IDC-NL, F.Cu at (208.5, 93.4)
- added Q1: DMG1013UWQ-7, arvsom-footprints:SOT-323, F.Cu at (215.3, 90.9)
- added Q5: DMG1012UW, arvsom-footprints:SOT-323, F.Cu at (235.9, 90.9)
- added R127: R_100k_0402, arvsom-footprints:0402-res, F.Cu at (218.8, 89.9)
- added R128: R_33R_0402, arvsom-footprints:0402-res, F.Cu at (214.8, 94.0)
- added R129: R_1k_0402, arvsom-footprints:0402-res, F.Cu at (239.4, 92.4)
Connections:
- J3 pad 93: nRPIBOOT -> BOOT_FROM_UARTn
- R53 pad 2: GND -> Net-(R53-Pad2)
- TP13 pad 1: /VIC7100 config/ATEMP_TEST0 -> Net-(TP13-Pad1)
- TP14 pad 1: /VIC7100 config/ATEMP_TEST1 -> Net-(TP14-Pad1)
- TP15 pad 1: /VIC7100 config/ATEMP_VSS -> Net-(TP15-Pad1)
- TP16 pad 1: /VIC7100 config/ATEMP_VCAL -> Net-(TP16-Pad1)
